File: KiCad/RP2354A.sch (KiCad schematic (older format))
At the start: 12 parts, among them J11 Conn_01x02, J16 USB_C_Receptacle_USB2.0, SW1 SW_Push, U16 RP2354A, Y1 ABM8-272-T3

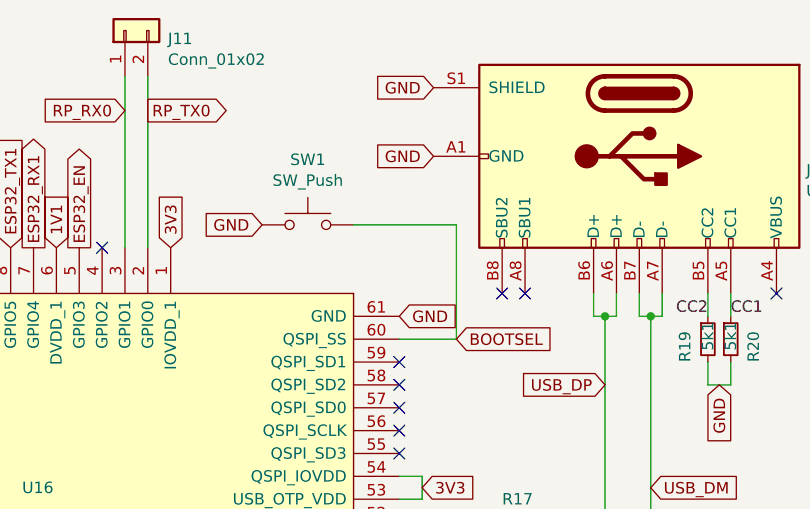
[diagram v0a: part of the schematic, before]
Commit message: Add a 1k series resistor on the BOOTSEL button to limit how hard we’re pulling on a line that’s also the active chip-select for the flash
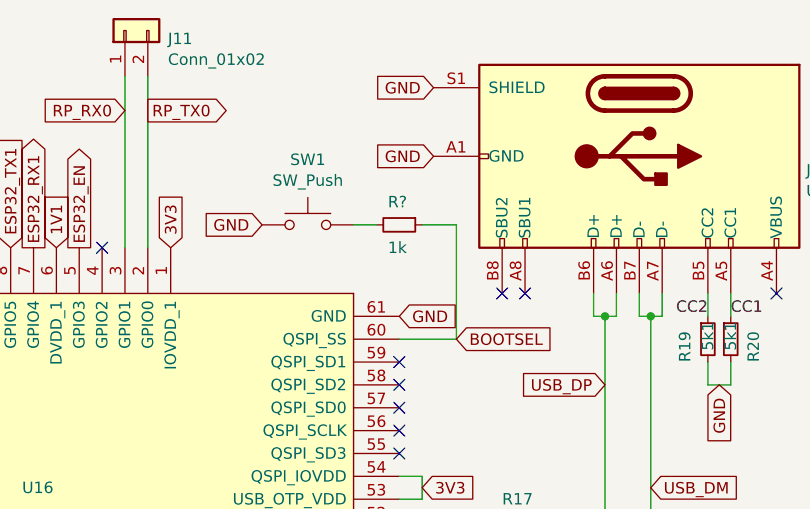
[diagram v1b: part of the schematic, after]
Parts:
- added R?: 1k, Resistor_SMD:R_0603_1608Metric_Pad0.98x0.95mm_HandSolder, symbol Device:R_Small
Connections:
- net BOOTSEL: now also R?.1; no longer SW1.2
- new net: R?.2, SW1.2
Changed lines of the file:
@@
 Wire Wire Line
 	7150 2800 7150 2300
-Wire Wire Line
-	7150 2300 6700 2300
 Text GLabel 6300 2300 0    50   Input ~ 0
 GND
+$Comp
+L Device:R_Small R?
+U 1 1 6AE48264
+P 6900 2300
+AR Path="/6AE48264" Ref="R?"  Part="1"
+AR Path="/6AFE5B10/6AE48264" Ref="R?"  Part="1"
+F 0 "R?" V 6800 2250 50  0000 L CNN
+F 1 "1k" V 7000 2250 50  0000 L CNN
+F 2 "Resistor_SMD:R_0603_1608Metric_Pad0.98x0.95mm_HandSolder" H 6900 2300 50  0001 C CNN
+F 3 "~" H 6900 2300 50  0001 C CNN
+	1    6900 2300
+	0    1    1    0
+$EndComp
+Wire Wire Line
+	7000 2300 7150 2300
+Wire Wire Line
+	6800 2300 6700 2300
 $EndSCHEMATC

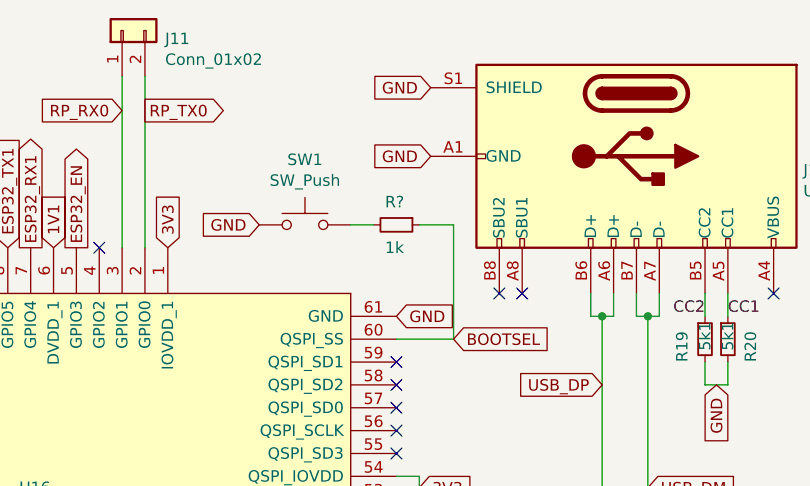
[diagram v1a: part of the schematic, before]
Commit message: Add decoupling caps for pin 31,42 on U7 (SN74LVC16245)
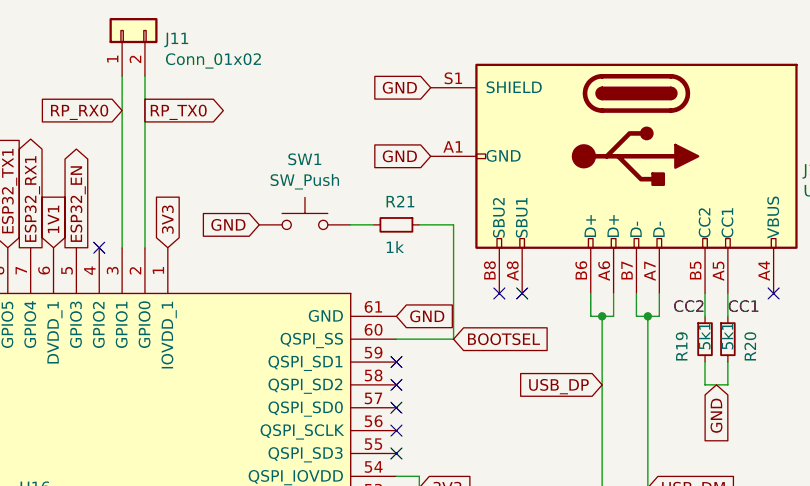
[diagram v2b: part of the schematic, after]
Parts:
- gave numbers to parts that had none: 1
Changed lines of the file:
@@
 P 6900 2300
 AR Path="/6AE48264" Ref="R?"  Part="1"
-AR Path="/6AFE5B10/6AE48264" Ref="R?"  Part="1"
-F 0 "R?" V 6800 2250 50  0000 L CNN
+AR Path="/6AFE5B10/6AE48264" Ref="R21"  Part="1"
+F 0 "R21" V 6800 2250 50  0000 L CNN
 F 1 "1k" V 7000 2250 50  0000 L CNN
 F 2 "Resistor_SMD:R_0603_1608Metric_Pad0.98x0.95mm_HandSolder" H 6900 2300 50  0001 C CNN

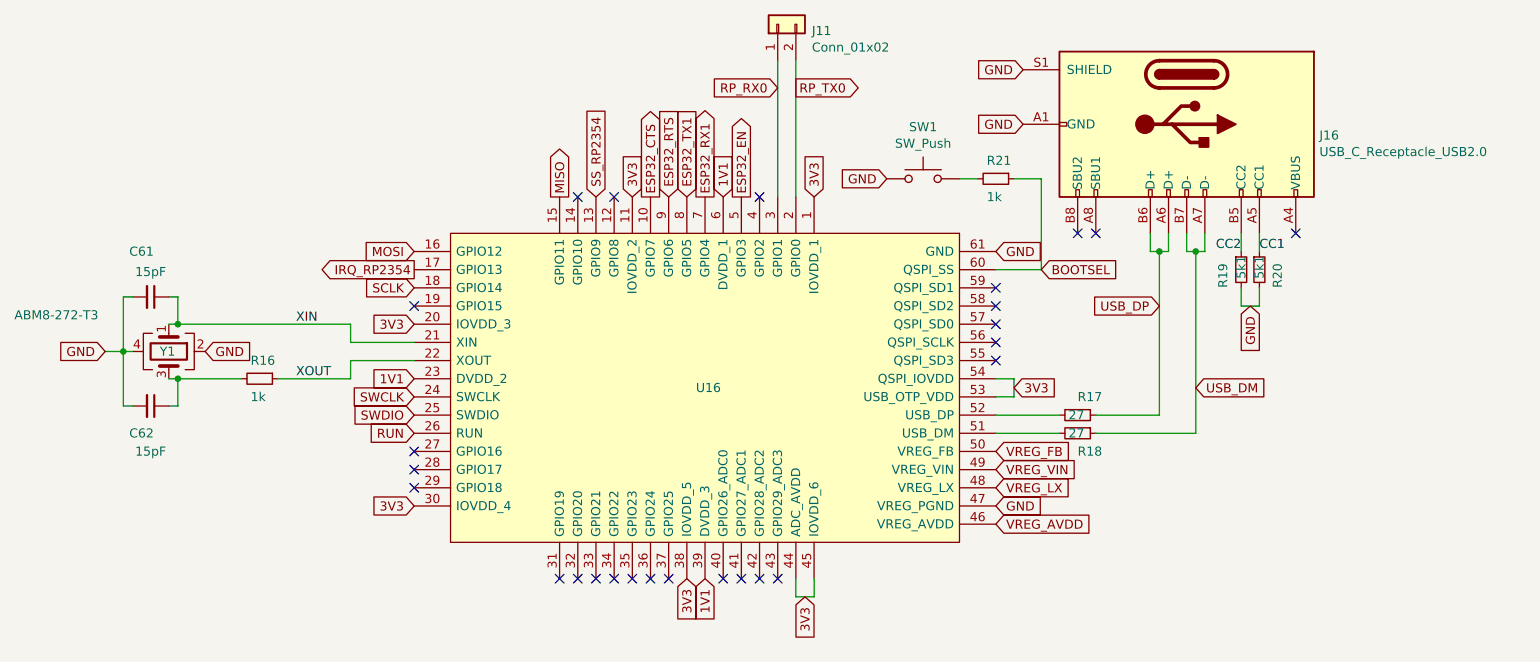
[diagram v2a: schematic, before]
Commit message: Update C34,C35,C39 to 1206 4.7uF size and move to be used in RP2354A power circuit. Add a 33 Ohm series resistor on VREG_AVDD and use C34 for decoupling of the same.
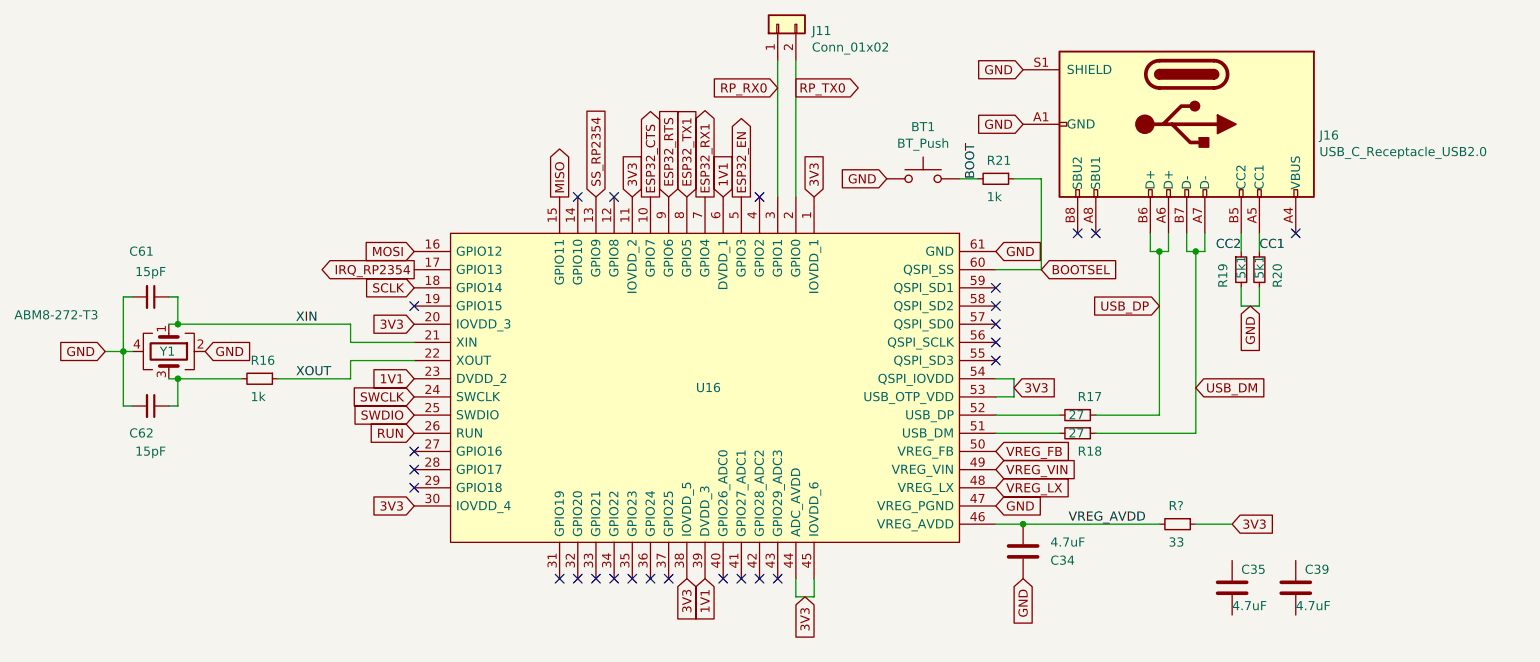
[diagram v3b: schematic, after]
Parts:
- added C34, C35, C39: 4.7uF, Capacitor_SMD:C_1206_3216Metric_Pad1.33x1.80mm_HandSolder, symbol Device:C
- added R?: 33, Resistor_SMD:R_0603_1608Metric_Pad0.98x0.95mm_HandSolder, symbol Device:R_Small
- BT1: renamed from SW1; value SW_Push -> BT_Push
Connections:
- net 3V3: now also R?.1
- net GND: now also C34.2
- net VREG_AVDD: now also C34.1, R?.2
- net BOOT: now reaches BT1.2, R21.2
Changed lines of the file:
@@
 Text GLabel 6900 4000 2    50   Input ~ 0
 VREG_LX
-Text GLabel 6900 4200 2    50   Input ~ 0
-VREG_AVDD
 Text GLabel 6900 4100 2    50   Input ~ 0
 GND
@@
 	8000 2700 8050 2700
 $Comp
-L Switch:SW_Push SW1
+L Switch:SW_Push BT1
 U 1 1 6AE2E6BB
 P 6500 2300
-F 0 "SW1" H 6500 2585 50  0000 C CNN
-F 1 "SW_Push" H 6500 2494 50  0000 C CNN
+F 0 "BT1" H 6500 2585 50  0000 C CNN
+F 1 "BT_Push" H 6500 2494 50  0000 C CNN
 F 2 "SF2000:Sunrom_Tactile_Switch_3x4x2mm_SMD_2-Pin" H 6500 2500 50  0001 C CNN
 F 3 "~" H 6500 2500 50  0001 C CNN
@@
 Wire Wire Line
 	6800 2300 6700 2300
+Text Label 6800 2300 1    50   ~ 0
+BOOT
+$Comp
+L Device:C C?
+U 1 1 6AF78685
+P 7050 4350
+AR Path="/6AF78685" Ref="C?"  Part="1"
+AR Path="/6AFE5B10/6AF78685" Ref="C34"  Part="1"
+F 0 "C34" H 7200 4300 50  0000 L CNN
+F 1 "4.7uF" H 7200 4400 50  0000 L CNN
+F 2 "Capacitor_SMD:C_1206_3216Metric_Pad1.33x1.80mm_HandSolder" H 7088 4200 50  0001 C CNN
+F 3 "~" H 7050 4350 50  0001 C CNN
+	1    7050 4350
+	1    0    0    -1
+$EndComp
+$Comp
+L Device:C C?
+U 1 1 6AF91B11
+P 8200 4550
+AR Path="/6AF91B11" Ref="C?"  Part="1"
+AR Path="/6AFE5B10/6AF91B11" Ref="C35"  Part="1"
+F 0 "C35" H 8250 4650 50  0000 L CNN
+F 1 "4.7uF" H 8200 4450 50  0000 L CNN
+F 2 "Capacitor_SMD:C_1206_3216Metric_Pad1.33x1.80mm_HandSolder" H 8238 4400 50  0001 C CNN
+F 3 "~" H 8200 4550 50  0001 C CNN
+	1    8200 4550
+	1    0    0    -1
+$EndComp
+$Comp
+L Device:C C?
+U 1 1 6AFADC4E
+P 8550 4550
+AR Path="/6AFADC4E" Ref="C?"  Part="1"
+AR Path="/6AFE5B10/6AFADC4E" Ref="C39"  Part="1"
+F 0 "C39" H 8600 4650 50  0000 L CNN
+F 1 "4.7uF" H 8550 4450 50  0000 L CNN
+F 2 "Capacitor_SMD:C_1206_3216Metric_Pad1.33x1.80mm_HandSolder" H 8588 4400 50  0001 C CNN
+F 3 "~" H 8550 4550 50  0001 C CNN
+	1    8550 4550
+	1    0    0    -1
+$EndComp
+Wire Wire Line
+	6900 4200 7050 4200
+Connection ~ 7050 4200
+Wire Wire Line
+	7050 4200 7800 4200
+Text Label 7300 4200 0    50   ~ 0
+VREG_AVDD
+Text GLabel 7050 4500 3    50   Input ~ 0
+GND
+$Comp
+L Device:R_Small R?
+U 1 1 6AFDAD5A
+P 7900 4200
+AR Path="/6AFDAD5A" Ref="R?"  Part="1"
+AR Path="/6AFE5B10/6AFDAD5A" Ref="R?"  Part="1"
+F 0 "R?" V 7800 4150 50  0000 L CNN
+F 1 "33" V 8000 4150 50  0000 L CNN
+F 2 "Resistor_SMD:R_0603_1608Metric_Pad0.98x0.95mm_HandSolder" H 7900 4200 50  0001 C CNN
+F 3 "~" H 7900 4200 50  0001 C CNN
+	1    7900 4200
+	0    1    1    0
+$EndComp
+Text GLabel 8200 4200 2    50   Input ~ 0
+3V3
+Wire Wire Line
+	8200 4200 8000 4200
 $EndSCHEMATC

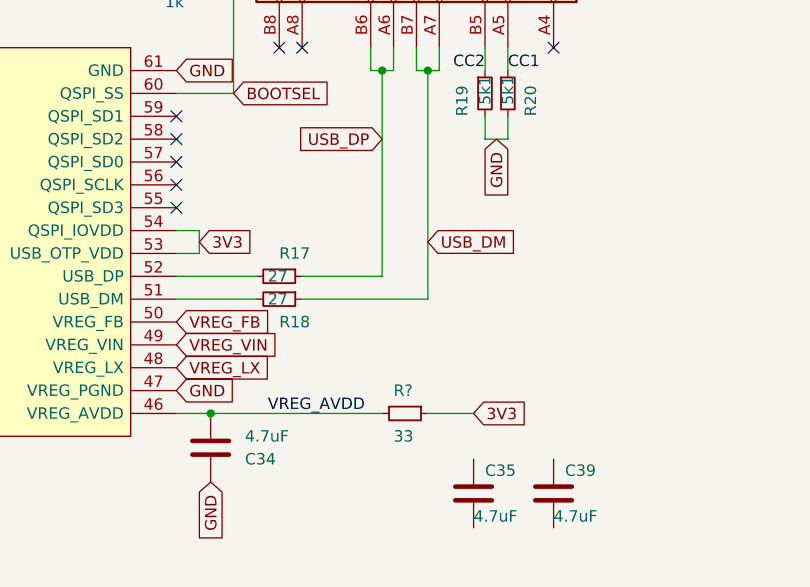
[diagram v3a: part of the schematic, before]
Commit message: Use C35 for VREG_VIN
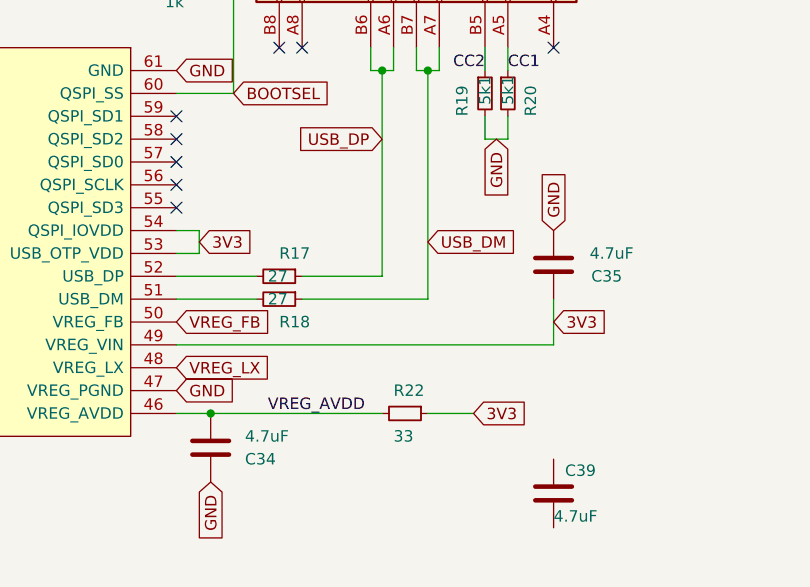
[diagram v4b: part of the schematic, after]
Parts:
- gave numbers to parts that had none: 1
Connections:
- net VREG_VIN is gone; now on net 3V3: U16.49 (VREG_VIN)
- net 3V3: now also C35.1
- net GND: now also C35.2
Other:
- moved on the sheet: C35
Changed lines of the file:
@@
 Text GLabel 6900 3800 2    50   Input ~ 0
 VREG_FB
-Text GLabel 6900 3900 2    50   Input ~ 0
-VREG_VIN
 Text GLabel 6900 4000 2    50   Input ~ 0
 VREG_LX
@@
 L Device:C C?
 U 1 1 6AF91B11
-P 8200 4550
+P 8550 3550
 AR Path="/6AF91B11" Ref="C?"  Part="1"
 AR Path="/6AFE5B10/6AF91B11" Ref="C35"  Part="1"
-F 0 "C35" H 8250 4650 50  0000 L CNN
-F 1 "4.7uF" H 8200 4450 50  0000 L CNN
-F 2 "Capacitor_SMD:C_1206_3216Metric_Pad1.33x1.80mm_HandSolder" H 8238 4400 50  0001 C CNN
-F 3 "~" H 8200 4550 50  0001 C CNN
-	1    8200 4550
-	1    0    0    -1
+F 0 "C35" H 8250 3600 50  0000 L CNN
+F 1 "4.7uF" H 8200 3500 50  0000 L CNN
+F 2 "Capacitor_SMD:C_1206_3216Metric_Pad1.33x1.80mm_HandSolder" H 8588 3400 50  0001 C CNN
+F 3 "~" H 8550 3550 50  0001 C CNN
+	1    8550 3550
+	-1   0    0    1
 $EndComp
 $Comp
@@
 P 7900 4200
 AR Path="/6AFDAD5A" Ref="R?"  Part="1"
-AR Path="/6AFE5B10/6AFDAD5A" Ref="R?"  Part="1"
-F 0 "R?" V 7800 4150 50  0000 L CNN
+AR Path="/6AFE5B10/6AFDAD5A" Ref="R22"  Part="1"
+F 0 "R22" V 7800 4150 50  0000 L CNN
 F 1 "33" V 8000 4150 50  0000 L CNN
 F 2 "Resistor_SMD:R_0603_1608Metric_Pad0.98x0.95mm_HandSolder" H 7900 4200 50  0001 C CNN
@@
 Wire Wire Line
 	8200 4200 8000 4200
+Wire Wire Line
+	6900 3900 8550 3900
+Wire Wire Line
+	8550 3900 8550 3700
+Text GLabel 8550 3400 1    50   Input ~ 0
+GND
+Text GLabel 8550 3800 2    50   Input ~ 0
+3V3
 $EndSCHEMATC

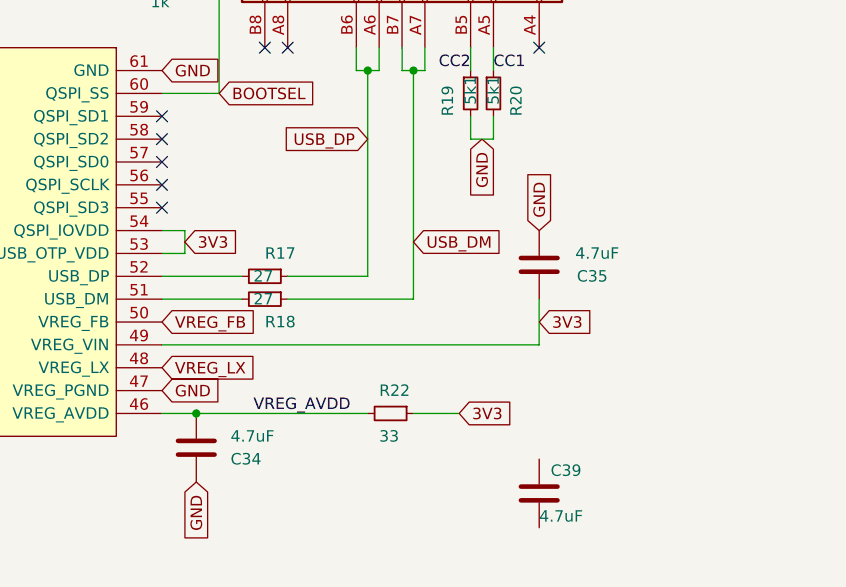
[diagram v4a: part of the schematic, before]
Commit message: Place C39 for VREG_FB
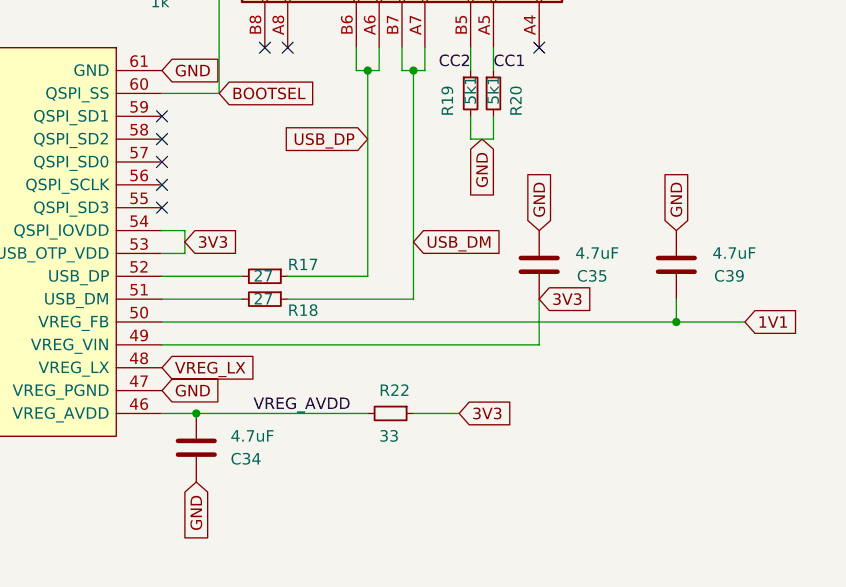
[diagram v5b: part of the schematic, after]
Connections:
- net VREG_FB is gone; now on net 1V1: U16.50 (VREG_FB)
- net 1V1: now also C39.1
- net GND: now also C39.2
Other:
- moved on the sheet: C39
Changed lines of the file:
@@
 Text GLabel 3700 3700 0    50   Input ~ 0
 RUN
-Text GLabel 6900 3800 2    50   Input ~ 0
-VREG_FB
 Text GLabel 6900 4000 2    50   Input ~ 0
 VREG_LX
@@
 AR Path="/6ADC9F07" Ref="R?"  Part="1"
 AR Path="/6AFE5B10/6ADC9F07" Ref="R17"  Part="1"
-F 0 "R17" V 7250 3600 50  0000 L CNN
+F 0 "R17" V 7300 3700 50  0000 L CNN
 F 1 "27" V 7350 3550 50  0000 L CNN
 F 2 "Resistor_SMD:R_0603_1608Metric_Pad0.98x0.95mm_HandSolder" H 7350 3600 50  0001 C CNN
@@
 AR Path="/6ADD8B0E" Ref="R?"  Part="1"
 AR Path="/6AFE5B10/6ADD8B0E" Ref="R18"  Part="1"
-F 0 "R18" V 7450 3700 50  0000 L CNN
+F 0 "R18" V 7400 3800 50  0000 L CNN
 F 1 "27" V 7350 3650 50  0000 L CNN
 F 2 "Resistor_SMD:R_0603_1608Metric_Pad0.98x0.95mm_HandSolder" H 7350 3700 50  0001 C CNN
@@
 L Device:C C?
 U 1 1 6AFADC4E
-P 8550 4550
+P 9150 3550
 AR Path="/6AFADC4E" Ref="C?"  Part="1"
 AR Path="/6AFE5B10/6AFADC4E" Ref="C39"  Part="1"
-F 0 "C39" H 8600 4650 50  0000 L CNN
-F 1 "4.7uF" H 8550 4450 50  0000 L CNN
-F 2 "Capacitor_SMD:C_1206_3216Metric_Pad1.33x1.80mm_HandSolder" H 8588 4400 50  0001 C CNN
-F 3 "~" H 8550 4550 50  0001 C CNN
-	1    8550 4550
-	1    0    0    -1
+F 0 "C39" H 8850 3600 50  0000 L CNN
+F 1 "4.7uF" H 8800 3500 50  0000 L CNN
+F 2 "Capacitor_SMD:C_1206_3216Metric_Pad1.33x1.80mm_HandSolder" H 9188 3400 50  0001 C CNN
+F 3 "~" H 9150 3550 50  0001 C CNN
+	1    9150 3550
+	-1   0    0    1
 $EndComp
 Wire Wire Line
@@
 Wire Wire Line
 	6900 3900 8550 3900
-Wire Wire Line
-	8550 3900 8550 3700
 Text GLabel 8550 3400 1    50   Input ~ 0
 GND
-Text GLabel 8550 3800 2    50   Input ~ 0
+Text GLabel 8550 3700 2    50   Input ~ 0
 3V3
+Wire Wire Line
+	8550 3700 8550 3900
+Text GLabel 9150 3400 1    50   Input ~ 0
+GND
+Text GLabel 9450 3800 2    50   Input ~ 0
+1V1
+Wire Wire Line
+	9450 3800 9150 3800
+Wire Wire Line
+	9150 3700 9150 3800
+Connection ~ 9150 3800
+Wire Wire Line
+	9150 3800 6900 3800
 $EndSCHEMATC

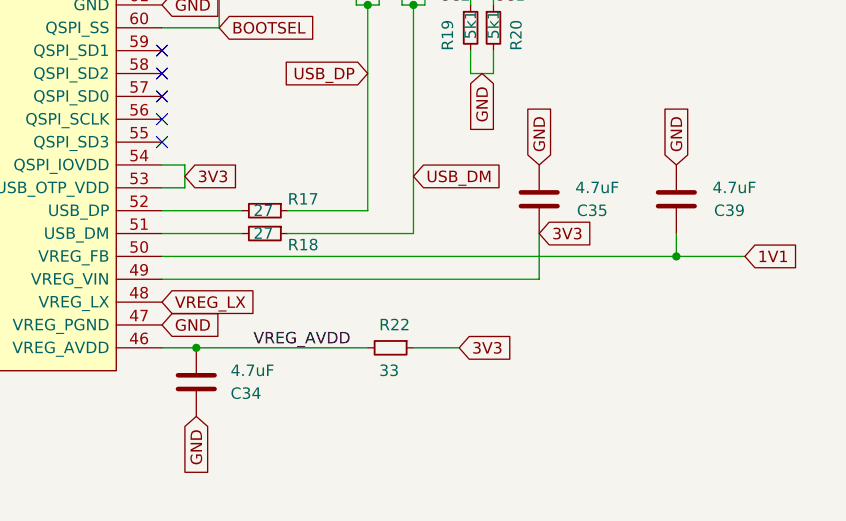
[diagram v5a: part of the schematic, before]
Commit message: Add recommended polarised inductor for RP2354A VREG_LX line and finish routing the remaining 1.1V power and 3.3V power to the RP
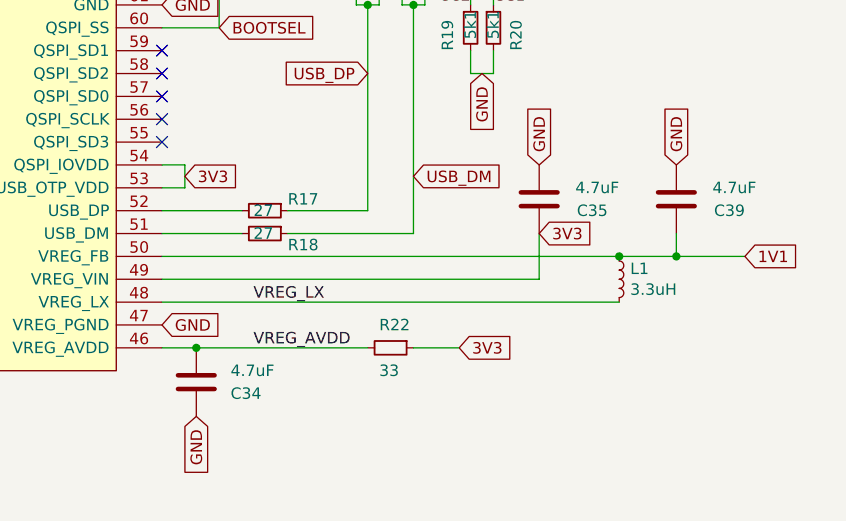
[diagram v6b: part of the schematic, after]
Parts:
- added L1: 3.3uH, SF2000:AOTAB201610S3R3101T, symbol Device:L_Small
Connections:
- net 1V1: now also L1.1
- net VREG_LX: now also L1.2
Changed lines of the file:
@@
 Text GLabel 3700 3700 0    50   Input ~ 0
 RUN
-Text GLabel 6900 4000 2    50   Input ~ 0
-VREG_LX
 Text GLabel 6900 4100 2    50   Input ~ 0
 GND
@@
 	9150 3700 9150 3800
 Connection ~ 9150 3800
-Wire Wire Line
-	9150 3800 6900 3800
+$Comp
+L Device:L_Small L1
+U 1 1 6B0133F1
+P 8900 3900
+F 0 "L1" H 8948 3946 50  0000 L CNN
+F 1 "3.3uH" H 8948 3855 50  0000 L CNN
+F 2 "SF2000:AOTAB201610S3R3101T" H 8900 3900 50  0001 C CNN
+F 3 "~" H 8900 3900 50  0001 C CNN
+	1    8900 3900
+	1    0    0    -1
+$EndComp
+Wire Wire Line
+	6900 3800 8900 3800
+Connection ~ 8900 3800
+Wire Wire Line
+	8900 3800 9150 3800
+Wire Wire Line
+	8900 4000 6900 4000
+Text Label 7300 4000 0    50   ~ 0
+VREG_LX
 $EndSCHEMATC
